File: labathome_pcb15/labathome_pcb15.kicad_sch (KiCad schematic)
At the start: 42 parts, among them J11 USB_ESP32, J15 CAN RS 485, J17 Micro_SD_Card_Det1, J21 GPIO, J22 Volts, J6 OneWire, J7 PROG, SW2 YELLOW, SW3 GREEN, SW3 Reset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

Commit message: labathome15 v0.0.1
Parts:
- J6: value OneWire -> I2C
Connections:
- net AO0 is gone; now on net GND: J6.4 (Pin_4)
- net OneWire is gone; now on net SDA: J6.2 (Pin_2)
- net +3V3: now also J21.3 (Pin_3)
- net 1wire: now also J21.4 (Pin_4)
- net GND: now also J21.1 (Pin_1), J21.2 (Pin_2); no longer J6.1 (Pin_1)
- net SCL: now also J6.1 (Pin_1)
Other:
- moved on the sheet: J21

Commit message: labathome_pcb15
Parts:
- R5: value k1 -> k22
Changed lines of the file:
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@@
 			)
 		)
-		(property "Value" "k1"
+		(property "Value" "k22"
 			(at 17.78 35.56 90)
 			(effects

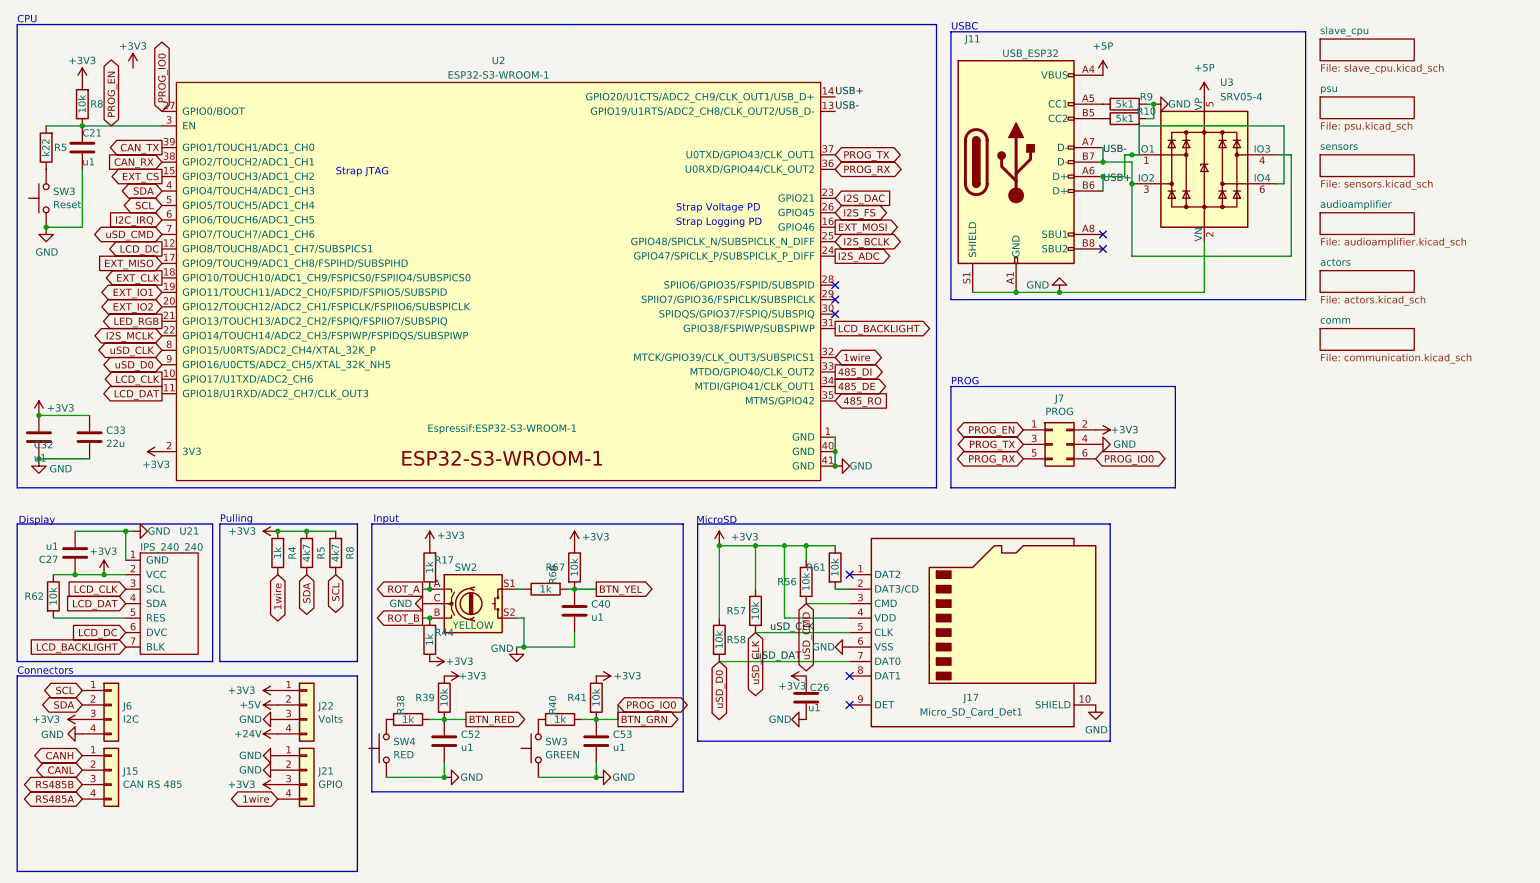
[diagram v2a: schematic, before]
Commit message: Various PCB and Code updates after review from Jana Marie Hemsing. Big Thankyou
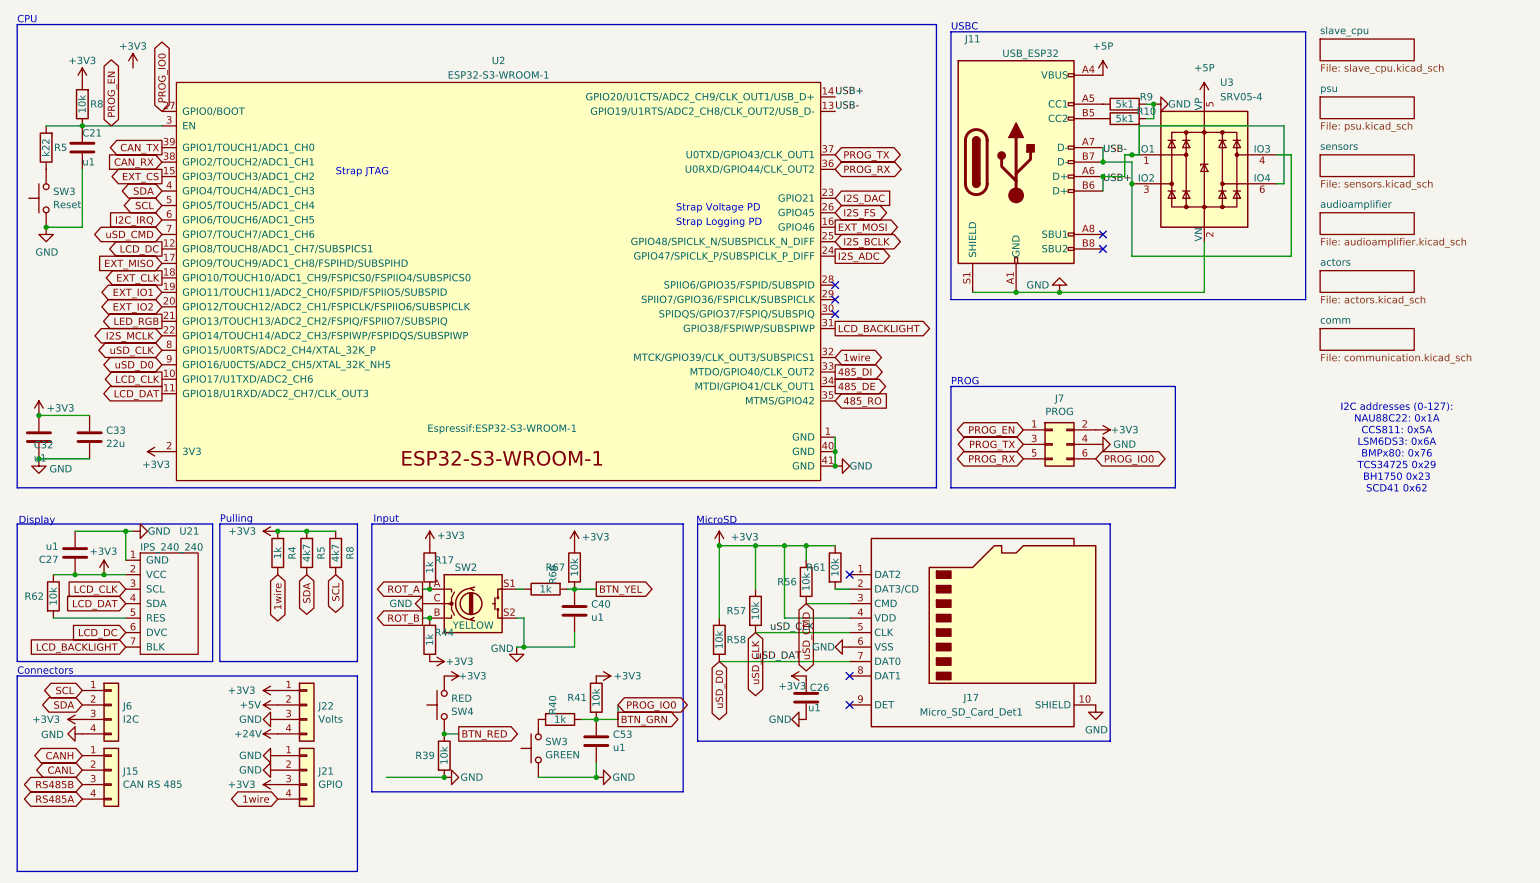
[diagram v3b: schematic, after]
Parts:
- removed C52: u1, Capacitor_SMD:C_0402_1005Metric, symbol Device:C
- removed R38: 1k, Resistor_SMD:R_0402_1005Metric, symbol Device:R
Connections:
- net +3V3: now also SW4.1; no longer R39.1
- net BTN_RED: now also R39.1, SW4.2; no longer R39.2
- net GND: now also R39.2; no longer SW4.1
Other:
- note added: "I2C addresses (0-127): NAU88C22: 0x1A CCS811: 0x5A LSM6DS3: 0x6A BMPx80: 0x76 TCS34725 0x29 BH1750 0x23 SCD41 0x62"
- moved on the sheet: R39, SW4
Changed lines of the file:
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@@
 	)
 	(junction
-		(at 87.63 135.89)
-		(diameter 0)
-		(color 0 0 0 0)
-	)
-	(junction
 		(at 16.51 82.55)
 		(diameter 0)
@@
 	)
 	(junction
+		(at 87.63 138.43)
+		(diameter 0)
+		(color 0 0 0 0)
+	)
+	(junction
 		(at 63.5 102.87)
 		(diameter 0)
@@
 		)
 	)
-	(wire
-		(pts
-			(xy 87.63 135.89) (xy 91.44 135.89)
-		)
-		(stroke
-			(width 0)
-			(type default)
-		)
-	)
 	(polyline
 		(pts
@@
 	(wire
 		(pts
-			(xy 85.09 135.89) (xy 87.63 135.89)
-		)
-		(stroke
-			(width 0)
-			(type default)
-		)
-	)
-	(wire
-		(pts
 			(xy 207.01 40.64) (xy 207.01 36.83)
 		)
@@
 	(wire
 		(pts
-			(xy 87.63 143.51) (xy 87.63 146.05)
+			(xy 87.63 138.43) (xy 90.17 138.43)
 		)
 		(stroke
@@
 		)
 	)
+	(text "I2C addresses (0-127):\nNAU88C22: 0x1A\nCCS811: 0x5A\nLSM6DS3: 0x6A\nBMPx80: 0x76\nTCS34725 0x29\nBH1750 0x23\nSCD41 0x62\n"
+		(exclude_from_sim no)
+		(at 254.762 88.392 0)
+		(effects
+			(font
+				(size 1.27 1.27)
+			)
+		)
+	)
 	(text "Pulling"
 		(exclude_from_sim no)
@@
 	(global_label "BTN_RED"
 		(shape output)
-		(at 91.44 135.89 0)
+		(at 90.17 138.43 0)
 		(fields_autoplaced yes)
 		(effects
@@
 		)
 		(property "Intersheetrefs" "${INTERSHEET_REFS}"
-			(at 102.6499 135.89 0)
+			(at 101.3799 138.43 0)
 			(effects
 				(font
@@
 	)
 	(symbol
-		(lib_id "Device:R")
-		(at 81.28 135.89 270)
-		(unit 1)
-		(exclude_from_sim no)
-		(in_bom yes)
-		(on_board yes)
-		(dnp no)
-		(property "Reference" "R38"
-			(at 80.01 133.35 0)
-			(effects
-				(font
-					(size 1.27 1.27)
-				)
-			)
-		)
-		(property "Value" "1k"
-			(at 81.28 135.89 90)
-			(effects
-				(font
-					(size 1.27 1.27)
-				)
-			)
-		)
-		(property "Footprint" "Resistor_SMD:R_0402_1005Metric"
-			(at 81.28 134.112 90)
-			(effects
-				(font
-					(size 1.27 1.27)
-				)
-				(hide yes)
-			)
-		)
-		(property "Datasheet" "~"
-			(at 81.28 135.89 0)
-			(effects
-				(font
-					(size 1.27 1.27)
-				)
-				(hide yes)
-			)
-		)
-		(property "Description" ""
-			(at 81.28 135.89 0)
-			(effects
-				(font
-					(size 1.27 1.27)
-				)
-				(hide yes)
-			)
-		)
-		(pin "1"
-		)
-		(pin "2"
-		)
-		(instances
-			(project "labathome_pcb15"
-				(path "/e4d6926a-1a8b-424d-97c4-66b6ad87e4ac"
-					(reference "R38")
-					(unit 1)
-				)
-			)
-		)
-	)
-	(symbol
 		(lib_id "power:GND")
 		(at 33.02 102.87 90)
@@
 	(symbol
 		(lib_id "Device:R")
-		(at 87.63 132.08 0)
+		(at 87.63 142.24 0)
 		(unit 1)
 		(exclude_from_sim no)
@@
 		(dnp no)
 		(property "Reference" "R39"
-			(at 82.55 132.08 0)
+			(at 82.55 142.24 0)
 			(effects
 				(font
@@
 		)
 		(property "Value" "10k"
-			(at 87.63 132.08 90)
+			(at 87.63 142.24 90)
 			(effects
 				(font
@@
 		)
 		(property "Footprint" "Resistor_SMD:R_0402_1005Metric"
-			(at 85.852 132.08 90)
+			(at 85.852 142.24 90)
 			(effects
 				(font
@@
 		)
 		(property "Datasheet" "~"
-			(at 87.63 132.08 0)
+			(at 87.63 142.24 0)
 			(effects
 				(font
@@
 		)
 		(property "Description" ""
-			(at 87.63 132.08 0)
+			(at 87.63 142.24 0)
 			(effects
 				(font
@@
 	(symbol
 		(lib_id "Switch:SW_Push")
-		(at 77.47 140.97 90)
+		(at 87.63 133.35 90)
+		(mirror x)
 		(unit 1)
 		(exclude_from_sim no)
@@
 		(dnp no)
 		(property "Reference" "SW4"
-			(at 78.6892 139.8016 90)
+			(at 88.8492 134.5184 90)
 			(effects
 				(font
@@
 		)
 		(property "Value" "RED"
-			(at 78.6892 142.113 90)
+			(at 88.8492 132.207 90)
 			(effects
 				(font
@@
 		)
 		(property "Footprint" "Button_Switch_THT:SW_PUSH-12mm"
-			(at 72.39 140.97 0)
+			(at 82.55 133.35 0)
 			(effects
 				(font
@@
 		)
 		(property "Datasheet" "~"
-			(at 72.39 140.97 0)
+			(at 82.55 133.35 0)
 			(effects
 				(font
@@
 		)
 		(property "Description" ""
-			(at 77.47 140.97 0)
+			(at 87.63 133.35 0)
 			(effects
 				(font
@@
 					(unit 1)
 				)
-			)
-		)
-	)
-	(symbol
-		(lib_id "Device:C")
-		(at 87.63 139.7 180)
-		(unit 1)
-		(exclude_from_sim no)
-		(in_bom yes)
-		(on_board yes)
-		(dnp no)
-		(property "Reference" "C52"
-			(at 90.551 138.5316 0)
-			(effects
-				(font
-					(size 1.27 1.27)
-				)
-				(justify right)
-			)
-		)
-		(property "Value" "u1"
-			(at 90.551 140.843 0)
-			(effects
-				(font
-					(size 1.27 1.27)
-				)
-				(justify right)
-			)
-		)
-		(property "Footprint" "Capacitor_SMD:C_0402_1005Metric"
-			(at 86.6648 135.89 0)
-			(effects
-				(font
-					(size 1.27 1.27)
-				)
-				(hide yes)
-			)
-		)
-		(property "Datasheet" "~"
-			(at 87.63 139.7 0)
-			(effects
-				(font
-					(size 1.27 1.27)
-				)
-				(hide yes)
-			)
-		)
-		(property "Description" ""
-			(at 87.63 139.7 0)
-			(effects
-				(font
-					(size 1.27 1.27)
-				)
-				(hide yes)
-			)
-		)
-		(pin "1"
-		)
-		(pin "2"
-		)
-		(instances
-			(project "labathome_pcb15"
-				(path "/e4d6926a-1a8b-424d-97c4-66b6ad87e4ac"
-					(reference "C52")
-					(unit 1)
-				)

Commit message: Further improventents in PCB layout
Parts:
- J11: symbol Connector:USB_C_Receptacle_USB2.0 -> Connector:USB_C_Receptacle_USB2.0_16P
- SW2: symbol Device:Rotary_Encoder_Switch -> Device:RotaryEncoder_Switch_MP
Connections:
- net GND: now also SW2.MP
- net I2S_DAC: now also U2.26 (GPIO45); no longer U2.23 (GPIO21)
- net I2S_FS: now also U2.23 (GPIO21); no longer U2.26 (GPIO45)

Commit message: Various Updates
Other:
- note added: "I2C addresses (0-127): AHT20: 0x38 BH1750 0x23 BMPx80: 0x76 CCS811: 0x5A LSM6DS3: 0x6A NAU88C22: 0x1A SCD41 0x62 TCS34725 0x29"
- note removed: "I2C addresses (0-127): NAU88C22: 0x1A CCS811: 0x5A LSM6DS3: 0x6A BMPx80: 0x76 TCS34725 0x29 BH1750 0x23 SCD41 0x62"
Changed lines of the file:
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@@
 		)
 	)
-	(text "I2C addresses (0-127):\nNAU88C22: 0x1A\nCCS811: 0x5A\nLSM6DS3: 0x6A\nBMPx80: 0x76\nTCS34725 0x29\nBH1750 0x23\nSCD41 0x62\n"
+	(text "I2C addresses (0-127):\nAHT20:  0x38\nBH1750 0x23\nBMPx80: 0x76\nCCS811: 0x5A\nLSM6DS3: 0x6A\nNAU88C22: 0x1A\nSCD41 0x62\nTCS34725 0x29\n"
 		(exclude_from_sim no)
 		(at 254.762 88.392 0)
